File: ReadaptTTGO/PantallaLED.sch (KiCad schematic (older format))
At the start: 1 part

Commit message: Primer aproximacion.
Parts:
- added C? (x6): 1uF, symbol Device:C
- added C?: 4.7uF, symbol Device:C
- added C?: 2.2uF, symbol Device:C
- added D?: D, symbol Device:D
- added R? (x3): 0R, symbol Device:R
- added R? (x2): 1k, symbol Device:R
- added R?: 910K, symbol Device:R
- added R? (x2): 4.7K, symbol Device:R
- added R?: R, symbol Device:R
- added U?: 662k, Package_TO_SOT_SMD:SOT-23, symbol Regulator_Linear:LM3480-3.3
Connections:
- net GND: now reaches U?.1 (NC(GND))
- net GND: now also U?.12 (BS2), U?.13 (CS#), U?.15 (D/C#), U?.16 (R/W#), U?.17 (E/RD#), U?.21 (D3), U?.22 (D4), U?.23 (D5), U?.24 (D6), U?.25 (D7), U?.29 (Vlss), U?.30 (NC(GND)), U?.8 (Vss), C?.2, C?.2, C?.2, C?.2, C?.2, C?.2, R?.1, R?.2, R?.2, U?.3 (GND)
- net at U?.10 (BS0): now also R?.1, R?.2
- net at U?.11 (BS1): now also R?.1, R?.2
- net RES: now reaches U?.14 (RES#)
- net RES: now also C?.1, D?.2 (A), R?.1
- net D0: now reaches U?.18 (D0/I2C_SCK)
- net D0: now also R?.2
- net D1: now reaches U?.19 (D1/I2C_SDA)
- net D1: now also R?.1, R?.2
- net at U?.2 (C2N): now also C?.1
- net D2: now reaches U?.20 (D2/I2C_SDA)
- net D2: now also R?.2
- net at U?.26 (Iref): now also R?.2
- net at U?.27 (Vcomh): now also C?.1
- net at U?.28 (Vcc): now also C?.1
- net at U?.3 (C2P): now also C?.2
- net at U?.4 (C1P): now also C?.1
- net at U?.5 (C1N): now also C?.2
- net VCC: now reaches U?.6 (Vbat)
- net VCC: now also U?.9 (Vdd), C?.1, C?.1, D?.1 (K), R?.1, R?.1, R?.1, R?.1, R?.2, U?.1 (VO)
- new net +3V3: C?.1, U?.2 (VI)
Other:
- moved on the sheet: U?

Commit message: Anotacciones
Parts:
- gave numbers to parts that had none: 20

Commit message: ERC completo
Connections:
- no-connect marks 0 -> 1
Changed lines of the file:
@@
 	1    0    0    -1
 $EndComp
+NoConn ~ 8650 2250
 $EndSCHEMATC

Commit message: Añadidos Footprints
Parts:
- C10, C11, C12, C13, C14, C9: footprint (none) -> Capacitor_SMD:C_01005_0402Metric
- C15, C16: footprint (none) -> Capacitor_SMD:C_0201_0603Metric
- D6: value D -> 1N4148; footprint (none) -> Diode_SMD:D_SOD-323
- R11, R12, R13, R14, R15, R16, R17, R18, R19: footprint (none) -> Resistor_SMD:R_01005_0402Metric
- U8: footprint (none) -> Connector_FFC-FPC:Molex_200528-0300_1x30-1MP_P1.00mm_Horizontal
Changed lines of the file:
@@
 F 0 "U8" H 10278 2746 50  0000 L CNN
 F 1 "OLED-128O064D" H 10278 2655 50  0000 L CNN
-F 2 "" V 8550 3400 50  0001 C CNN
+F 2 "Connector_FFC-FPC:Molex_200528-0300_1x30-1MP_P1.00mm_Horizontal" V 8550 3400 50  0001 C CNN
 F 3 "" V 8550 3400 50  0001 C CNN
 	1    9400 2900
@@
 F 0 "R15" H 7170 2246 50  0000 L CNN
 F 1 "0R" H 7170 2155 50  0000 L CNN
-F 2 "" V 7030 2200 50  0001 C CNN
+F 2 "Resistor_SMD:R_01005_0402Metric" V 7030 2200 50  0001 C CNN
 F 3 "~" H 7100 2200 50  0001 C CNN
 	1    7100 2200
@@
 F 0 "R17" H 7520 2246 50  0000 L CNN
 F 1 "1k" H 7520 2155 50  0000 L CNN
-F 2 "" V 7380 2200 50  0001 C CNN
+F 2 "Resistor_SMD:R_01005_0402Metric" V 7380 2200 50  0001 C CNN
 F 3 "~" H 7450 2200 50  0001 C CNN
 	1    7450 2200
@@
 F 0 "R18" H 7520 2946 50  0000 L CNN
 F 1 "0R" H 7520 2855 50  0000 L CNN
-F 2 "" V 7380 2900 50  0001 C CNN
+F 2 "Resistor_SMD:R_01005_0402Metric" V 7380 2900 50  0001 C CNN
 F 3 "~" H 7450 2900 50  0001 C CNN
 	1    7450 2900
@@
 F 0 "R16" H 7170 2946 50  0000 L CNN
 F 1 "1k" H 7170 2855 50  0000 L CNN
-F 2 "" V 7030 2900 50  0001 C CNN
+F 2 "Resistor_SMD:R_01005_0402Metric" V 7030 2900 50  0001 C CNN
 F 3 "~" H 7100 2900 50  0001 C CNN
 	1    7100 2900
@@
 F 0 "R19" V 8400 4200 50  0000 C CNN
 F 1 "910K" V 8300 4150 50  0000 C CNN
-F 2 "" V 8130 4150 50  0001 C CNN
+F 2 "Resistor_SMD:R_01005_0402Metric" V 8130 4150 50  0001 C CNN
 F 3 "~" H 8200 4150 50  0001 C CNN
 	1    8200 4150
@@
 F 0 "C13" H 7700 1750 50  0000 L CNN
 F 1 "1uF" H 7700 1650 50  0000 L CNN
-F 2 "" H 7988 1550 50  0001 C CNN
+F 2 "Capacitor_SMD:C_01005_0402Metric" H 7988 1550 50  0001 C CNN
 F 3 "~" H 7950 1700 50  0001 C CNN
 	1    7950 1700
@@
 F 0 "C14" H 7700 2150 50  0000 L CNN
 F 1 "1uF" H 7700 2050 50  0000 L CNN
-F 2 "" H 7988 1950 50  0001 C CNN
+F 2 "Capacitor_SMD:C_01005_0402Metric" H 7988 1950 50  0001 C CNN
 F 3 "~" H 7950 2100 50  0001 C CNN
 	1    7950 2100
@@
 F 0 "C16" H 8250 4600 50  0000 L CNN
 F 1 "2.2uF" H 8250 4500 50  0000 L CNN
-F 2 "" H 8238 4550 50  0001 C CNN
+F 2 "Capacitor_SMD:C_0201_0603Metric" H 8238 4550 50  0001 C CNN
 F 3 "~" H 8200 4700 50  0001 C CNN
 	1    8200 4700
@@
 F 0 "C15" H 7750 4600 50  0000 L CNN
 F 1 "4.7uF" H 7700 4500 50  0000 L CNN
-F 2 "" H 7988 4550 50  0001 C CNN
+F 2 "Capacitor_SMD:C_0201_0603Metric" H 7988 4550 50  0001 C CNN
 F 3 "~" H 7950 4700 50  0001 C CNN
 	1    7950 4700
@@
 F 0 "C11" H 4750 1750 50  0000 L CNN
 F 1 "1uF" H 4750 1650 50  0000 L CNN
-F 2 "" H 5038 1550 50  0001 C CNN
+F 2 "Capacitor_SMD:C_01005_0402Metric" H 5038 1550 50  0001 C CNN
 F 3 "~" H 5000 1700 50  0001 C CNN
 	1    5000 1700
@@
 F 0 "C12" H 5150 1750 50  0000 L CNN
 F 1 "1uF" H 5150 1650 50  0000 L CNN
-F 2 "" H 5438 1550 50  0001 C CNN
+F 2 "Capacitor_SMD:C_01005_0402Metric" H 5438 1550 50  0001 C CNN
 F 3 "~" H 5400 1700 50  0001 C CNN
 	1    5400 1700
@@
 F 0 "R14" H 5450 3450 50  0000 C CNN
 F 1 "0R" H 5450 3550 50  0000 C CNN
-F 2 "" V 5480 3500 50  0001 C CNN
+F 2 "Resistor_SMD:R_01005_0402Metric" V 5480 3500 50  0001 C CNN
 F 3 "~" H 5550 3500 50  0001 C CNN
 	1    5550 3500
@@
 F 0 "R13" H 5300 3450 50  0000 C CNN
 F 1 "4.7K" H 5350 3550 50  0000 C CNN
-F 2 "" V 5130 3500 50  0001 C CNN
+F 2 "Resistor_SMD:R_01005_0402Metric" V 5130 3500 50  0001 C CNN
 F 3 "~" H 5200 3500 50  0001 C CNN
 	1    5200 3500
@@
 F 0 "R12" H 5050 3450 50  0000 C CNN
 F 1 "4.7K" H 5050 3550 50  0000 C CNN
-F 2 "" V 4780 3500 50  0001 C CNN
+F 2 "Resistor_SMD:R_01005_0402Metric" V 4780 3500 50  0001 C CNN
 F 3 "~" H 4850 3500 50  0001 C CNN
 	1    4850 3500
@@
 F 0 "C9" H 1500 1650 50  0000 L CNN
 F 1 "1uF" H 1500 1550 50  0000 L CNN
-F 2 "" H 1788 1450 50  0001 C CNN
+F 2 "Capacitor_SMD:C_01005_0402Metric" H 1788 1450 50  0001 C CNN
 F 3 "~" H 1750 1600 50  0001 C CNN
 	1    1750 1600
@@
 F 0 "R11" H 2620 4096 50  0000 L CNN
 F 1 "R" H 2620 4005 50  0000 L CNN
-F 2 "" V 2480 4050 50  0001 C CNN
+F 2 "Resistor_SMD:R_01005_0402Metric" V 2480 4050 50  0001 C CNN
 F 3 "~" H 2550 4050 50  0001 C CNN
 	1    2550 4050
@@
 P 2950 4050
 F 0 "D6" V 2996 3971 50  0000 R CNN
-F 1 "D" V 2905 3971 50  0000 R CNN
-F 2 "" H 2950 4050 50  0001 C CNN
+F 1 "1N4148" V 2905 3971 50  0000 R CNN
+F 2 "Diode_SMD:D_SOD-323" H 2950 4050 50  0001 C CNN
 F 3 "~" H 2950 4050 50  0001 C CNN
 	1    2950 4050
@@
 F 0 "C10" H 1800 4100 50  0000 L CNN
 F 1 "1uF" H 1800 4000 50  0000 L CNN
-F 2 "" H 2088 3900 50  0001 C CNN
+F 2 "Capacitor_SMD:C_01005_0402Metric" H 2088 3900 50  0001 C CNN
 F 3 "~" H 2050 4050 50  0001 C CNN
 	1    2050 4050

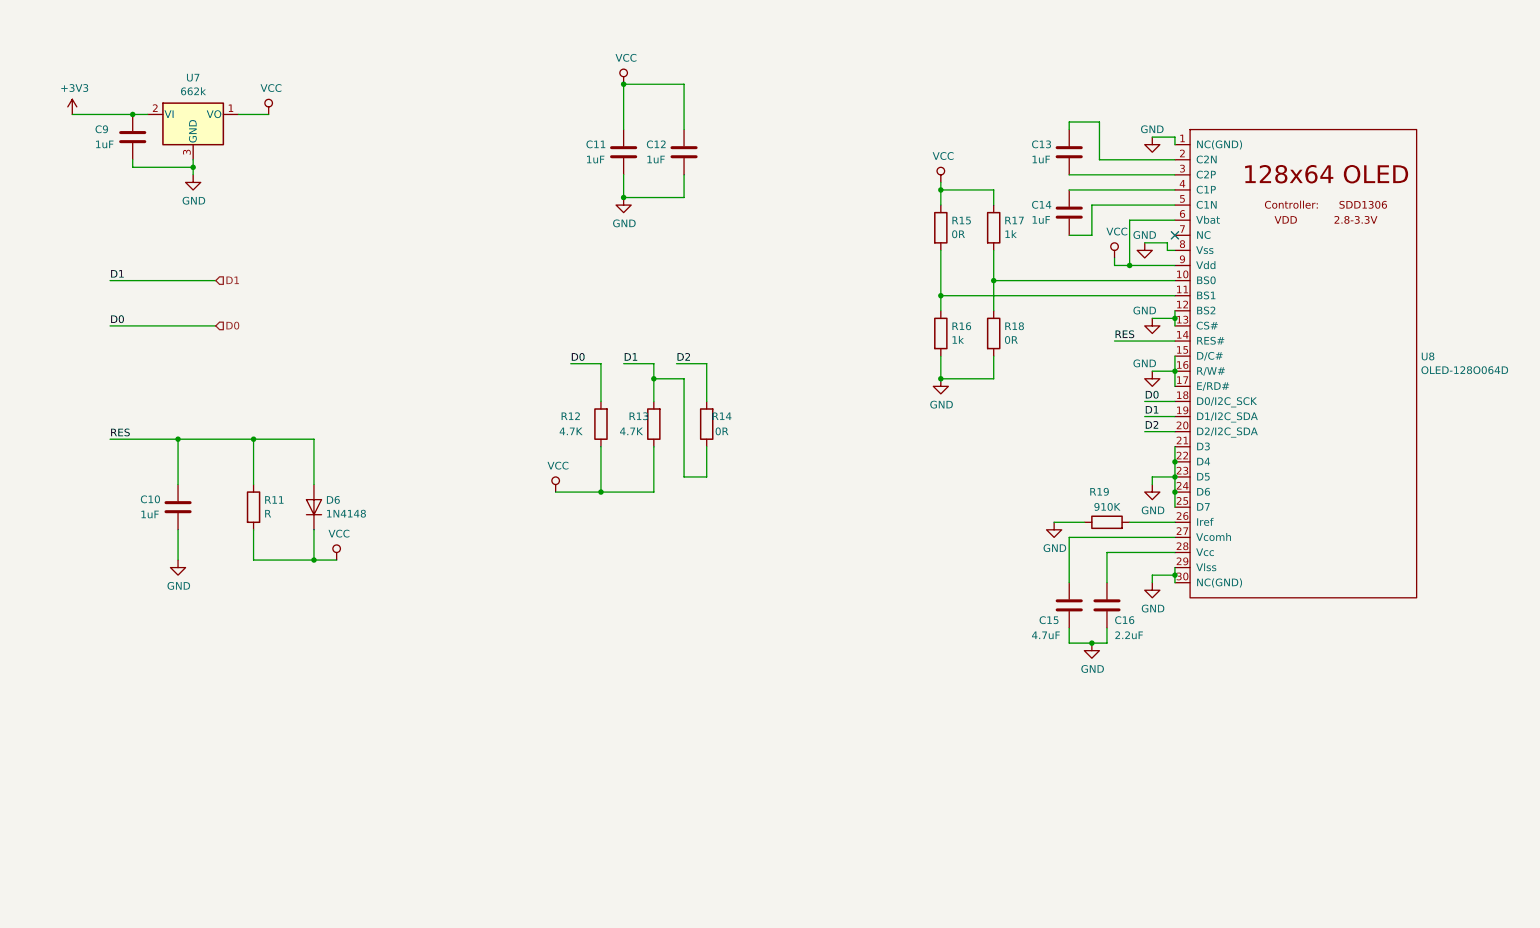
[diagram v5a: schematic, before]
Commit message: PCB sin traces
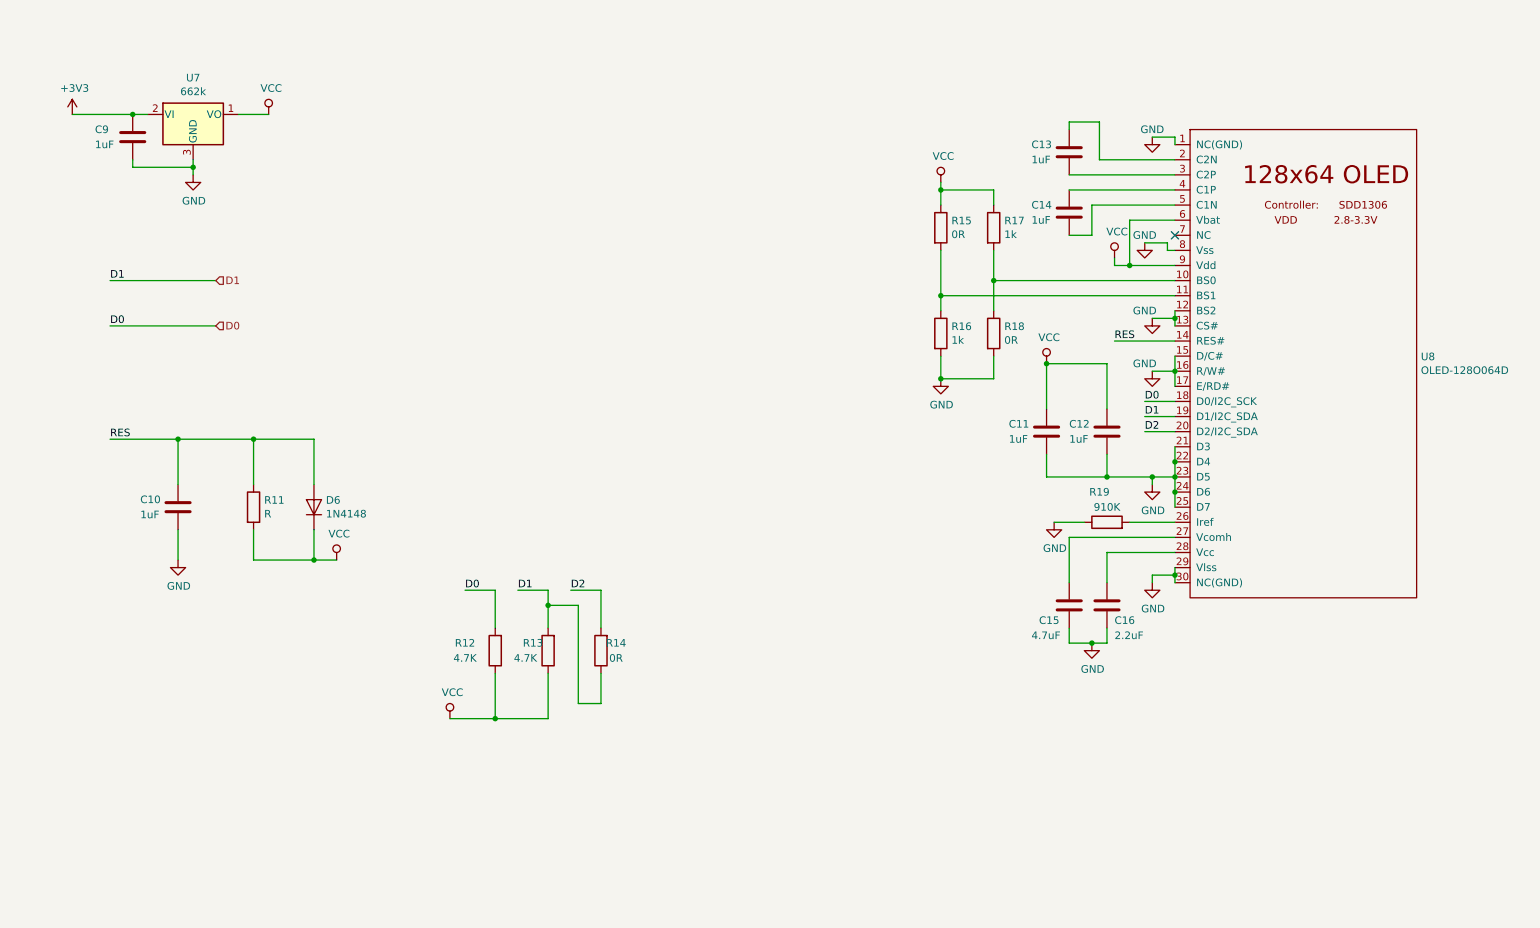
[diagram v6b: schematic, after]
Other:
- moved on the sheet: C11, C12, R12, R13, R14
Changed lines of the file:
@@
 	7850 4150 8050 4150
-$Comp
-L Device:C C?
-U 1 1 5D33C436
-P 5000 1700
-AR Path="/5D087535/5D33C436" Ref="C?"  Part="1"
-AR Path="/5D086AE7/5D33C436" Ref="C11"  Part="1"
-F 0 "C11" H 4750 1750 50  0000 L CNN
-F 1 "1uF" H 4750 1650 50  0000 L CNN
-F 2 "Capacitor_SMD:C_01005_0402Metric" H 5038 1550 50  0001 C CNN
-F 3 "~" H 5000 1700 50  0001 C CNN
-	1    5000 1700
-	1    0    0    -1
-$EndComp
-$Comp
-L Device:C C?
-U 1 1 5D341B01
-P 5400 1700
-AR Path="/5D087535/5D341B01" Ref="C?"  Part="1"
-AR Path="/5D086AE7/5D341B01" Ref="C12"  Part="1"
-F 0 "C12" H 5150 1750 50  0000 L CNN
-F 1 "1uF" H 5150 1650 50  0000 L CNN
-F 2 "Capacitor_SMD:C_01005_0402Metric" H 5438 1550 50  0001 C CNN
-F 3 "~" H 5400 1700 50  0001 C CNN
-	1    5400 1700
-	1    0    0    -1
-$EndComp
 $Comp
 L power:VCC #PWR0141
@@
 	8650 1650 8650 1600
 Wire Wire Line
-	5400 1850 5400 2000
-Wire Wire Line
-	5000 1550 5000 1250
-Wire Wire Line
-	5000 1850 5000 2000
-Wire Wire Line
-	5400 1250 5400 1550
-$Comp
-L power:GND #PWR0146
-U 1 1 5D3E3469
-P 5000 2000
-F 0 "#PWR0146" H 5000 1750 50  0001 C CNN
-F 1 "GND" H 5005 1827 50  0000 C CNN
-F 2 "" H 5000 2000 50  0001 C CNN
-F 3 "" H 5000 2000 50  0001 C CNN
-	1    5000 2000
-	1    0    0    -1
-$EndComp
-$Comp
-L power:VCC #PWR0147
-U 1 1 5D3EF749
-P 5000 1250
-F 0 "#PWR0147" H 5000 1100 50  0001 C CNN
-F 1 "VCC" H 5017 1423 50  0000 C CNN
-F 2 "" H 5000 1250 50  0001 C CNN
-F 3 "" H 5000 1250 50  0001 C CNN
-	1    5000 1250
-	1    0    0    -1
-$EndComp
-Wire Wire Line
-	5400 3200 5400 3850
-Wire Wire Line
-	5550 3650 5550 3850
-Connection ~ 4850 3950
-Wire Wire Line
-	4850 3950 4550 3950
+	4700 4700 4700 5350
+Wire Wire Line
+	4850 5150 4850 5350
+Connection ~ 4150 5450
+Wire Wire Line
+	4150 5450 3850 5450
 $Comp
 L power:VCC #PWR0148
 U 1 1 5D2CACB0
-P 4550 3950
-F 0 "#PWR0148" H 4550 3800 50  0001 C CNN
-F 1 "VCC" H 4567 4123 50  0000 C CNN
-F 2 "" H 4550 3950 50  0001 C CNN
-F 3 "" H 4550 3950 50  0001 C CNN
-	1    4550 3950
-	1    0    0    -1
-$EndComp
-Wire Wire Line
-	5200 3200 5200 3350
-Connection ~ 5200 3200
-Wire Wire Line
-	5400 3850 5550 3850
-Wire Wire Line
-	5200 3200 5400 3200
-Wire Wire Line
-	5200 3950 4850 3950
-Wire Wire Line
-	5200 3650 5200 3950
-Wire Wire Line
-	4850 3650 4850 3950
-Wire Wire Line
-	5550 3100 5550 3350
-Wire Wire Line
-	5200 3100 5200 3200
-Wire Wire Line
-	4850 3350 4850 3100
-Wire Wire Line
-	5200 3100 5000 3100
-Text Label 5000 3100 0    50   ~ 0
+P 3850 5450
+F 0 "#PWR0148" H 3850 5300 50  0001 C CNN
+F 1 "VCC" H 3867 5623 50  0000 C CNN
+F 2 "" H 3850 5450 50  0001 C CNN
+F 3 "" H 3850 5450 50  0001 C CNN
+	1    3850 5450
+	1    0    0    -1
+$EndComp
+Wire Wire Line
+	4500 4700 4500 4850
+Connection ~ 4500 4700
+Wire Wire Line
+	4700 5350 4850 5350
+Wire Wire Line
+	4500 4700 4700 4700
+Wire Wire Line
+	4500 5450 4150 5450
+Wire Wire Line
+	4500 5150 4500 5450
+Wire Wire Line
+	4150 5150 4150 5450
+Wire Wire Line
+	4850 4600 4850 4850
+Wire Wire Line
+	4500 4600 4500 4700
+Wire Wire Line
+	4150 4850 4150 4600
+Wire Wire Line
+	4500 4600 4300 4600
+Text Label 4300 4600 0    50   ~ 0
 D1
-Text Label 5350 3100 0    50   ~ 0
+Text Label 4650 4600 0    50   ~ 0
 D2
 $Comp
 L Device:R R14
 U 1 1 5D2BFFE9
-P 5550 3500
-F 0 "R14" H 5450 3450 50  0000 C CNN
-F 1 "0R" H 5450 3550 50  0000 C CNN
-F 2 "Resistor_SMD:R_01005_0402Metric" V 5480 3500 50  0001 C CNN
-F 3 "~" H 5550 3500 50  0001 C CNN
-	1    5550 3500
+P 4850 5000
+F 0 "R14" H 4750 4950 50  0000 C CNN
+F 1 "0R" H 4750 5050 50  0000 C CNN
+F 2 "Resistor_SMD:R_01005_0402Metric" V 4780 5000 50  0001 C CNN
+F 3 "~" H 4850 5000 50  0001 C CNN
+	1    4850 5000
 	-1   0    0    1
 $EndComp
@@
 L Device:R R13
 U 1 1 5D2BF3D4
-P 5200 3500
-F 0 "R13" H 5300 3450 50  0000 C CNN
-F 1 "4.7K" H 5350 3550 50  0000 C CNN
-F 2 "Resistor_SMD:R_01005_0402Metric" V 5130 3500 50  0001 C CNN
-F 3 "~" H 5200 3500 50  0001 C CNN
-	1    5200 3500
+P 4500 5000
+F 0 "R13" H 4600 4950 50  0000 C CNN
+F 1 "4.7K" H 4650 5050 50  0000 C CNN
+F 2 "Resistor_SMD:R_01005_0402Metric" V 4430 5000 50  0001 C CNN
+F 3 "~" H 4500 5000 50  0001 C CNN
+	1    4500 5000
 	-1   0    0    1
 $EndComp
@@
 L Device:R R12
 U 1 1 5D2BE882
-P 4850 3500
-F 0 "R12" H 5050 3450 50  0000 C CNN
-F 1 "4.7K" H 5050 3550 50  0000 C CNN
-F 2 "Resistor_SMD:R_01005_0402Metric" V 4780 3500 50  0001 C CNN
-F 3 "~" H 4850 3500 50  0001 C CNN
-	1    4850 3500
+P 4150 5000
+F 0 "R12" H 4350 4950 50  0000 C CNN
+F 1 "4.7K" H 4350 5050 50  0000 C CNN
+F 2 "Resistor_SMD:R_01005_0402Metric" V 4080 5000 50  0001 C CNN
+F 3 "~" H 4150 5000 50  0001 C CNN
+	1    4150 5000
 	-1   0    0    1
 $EndComp
 Wire Wire Line
-	5350 3100 5550 3100
-Wire Wire Line
-	4650 3100 4850 3100
-Text Label 4650 3100 0    50   ~ 0
+	4650 4600 4850 4600
+Wire Wire Line
+	3950 4600 4150 4600
+Text Label 3950 4600 0    50   ~ 0
 D0
-Connection ~ 5000 2000
-Wire Wire Line
-	5000 2000 5400 2000
-Connection ~ 5000 1250
-Wire Wire Line
-	5000 1250 5400 1250
 $Comp
 L Regulator_Linear:LM3480-3.3 U7
@@
 $EndComp
 NoConn ~ 8650 2250
+Wire Wire Line
+	7800 3100 8200 3100
+Connection ~ 7800 3100
+$Comp
+L power:VCC #PWR0147
+U 1 1 5D3EF749
+P 7800 3100
+F 0 "#PWR0147" H 7800 2950 50  0001 C CNN
+F 1 "VCC" H 7817 3273 50  0000 C CNN
+F 2 "" H 7800 3100 50  0001 C CNN
+F 3 "" H 7800 3100 50  0001 C CNN
+	1    7800 3100
+	1    0    0    -1
+$EndComp
+Wire Wire Line
+	8200 3100 8200 3400
+Wire Wire Line
+	7800 3700 7800 3850
+Wire Wire Line
+	7800 3400 7800 3100
+Wire Wire Line
+	8200 3700 8200 3850
+$Comp
+L Device:C C?
+U 1 1 5D341B01
+P 8200 3550
+AR Path="/5D087535/5D341B01" Ref="C?"  Part="1"
+AR Path="/5D086AE7/5D341B01" Ref="C12"  Part="1"
+F 0 "C12" H 7950 3600 50  0000 L CNN
+F 1 "1uF" H 7950 3500 50  0000 L CNN
+F 2 "Capacitor_SMD:C_01005_0402Metric" H 8238 3400 50  0001 C CNN
+F 3 "~" H 8200 3550 50  0001 C CNN
+	1    8200 3550
+	1    0    0    -1
+$EndComp
+$Comp
+L Device:C C?
+U 1 1 5D33C436
+P 7800 3550
+AR Path="/5D087535/5D33C436" Ref="C?"  Part="1"
+AR Path="/5D086AE7/5D33C436" Ref="C11"  Part="1"
+F 0 "C11" H 7550 3600 50  0000 L CNN
+F 1 "1uF" H 7550 3500 50  0000 L CNN
+F 2 "Capacitor_SMD:C_01005_0402Metric" H 7838 3400 50  0001 C CNN
+F 3 "~" H 7800 3550 50  0001 C CNN
+	1    7800 3550
+	1    0    0    -1
+$EndComp
+Wire Wire Line
+	8500 3850 8200 3850
+Connection ~ 8500 3850
+Connection ~ 8200 3850
+Wire Wire Line
+	7800 3850 8200 3850
 $EndSCHEMATC

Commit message: Entrega revision 1.2
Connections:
- net RES: now also R11.2; no longer R11.1
- net VCC: now also R11.1; no longer R11.2
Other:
- note added: "Circuitos del display OLED."
- moved on the sheet: C11, C12, C13, C14, C15, C16, C9, R15, R16, R17, R18, R19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
